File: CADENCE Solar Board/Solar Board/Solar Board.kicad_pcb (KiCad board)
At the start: 2 copper layers, 36 parts, among them J1 Conn_01x08, U1 INA230AIRGTT, U2 AD7414ARTZ-1REEL7, U3 OPT3001IDNPRQ1

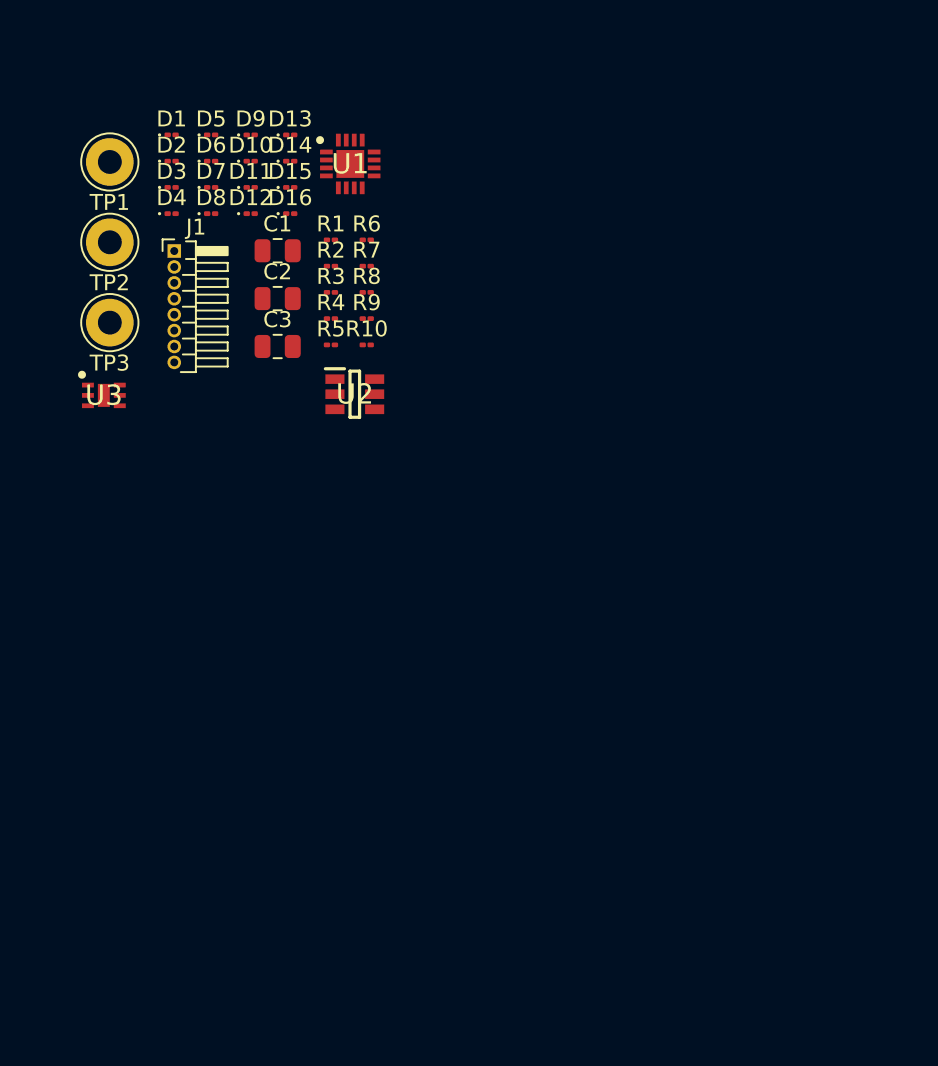
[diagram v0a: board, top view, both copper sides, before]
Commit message: fixed diodes
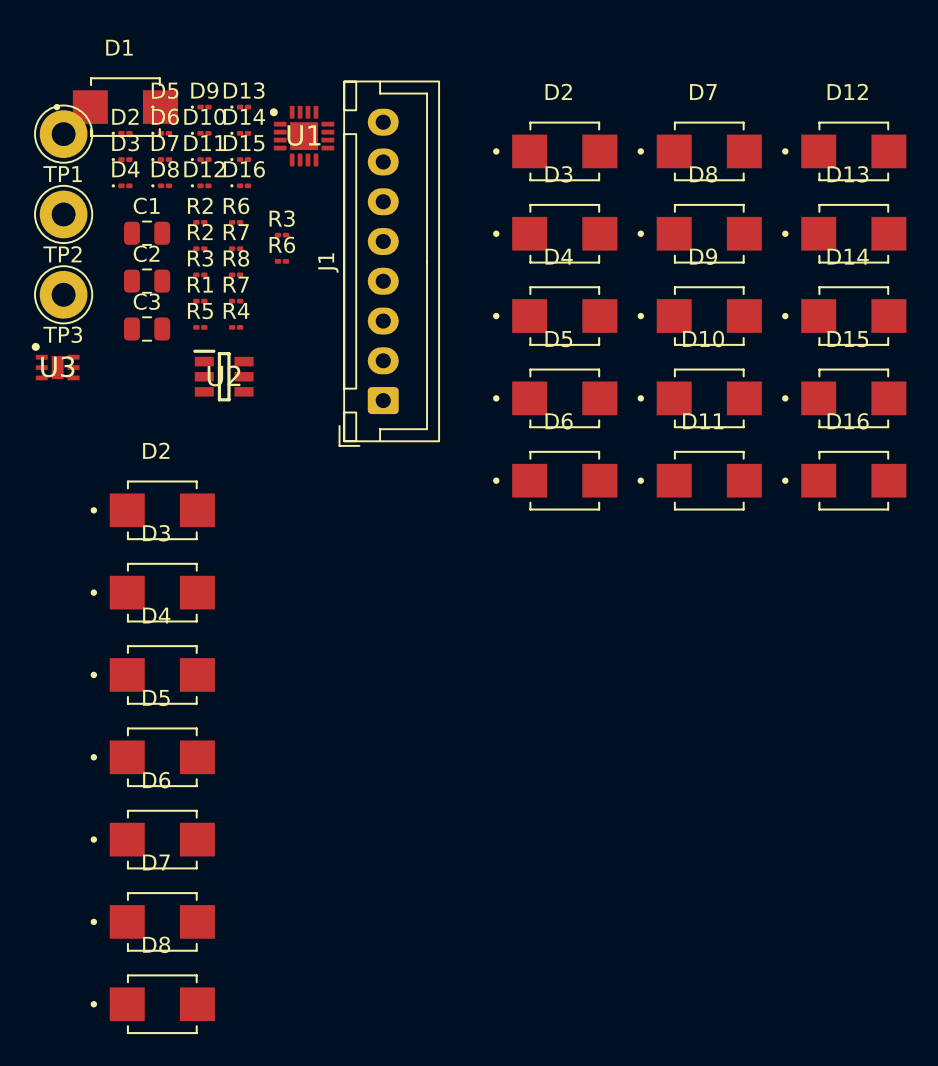
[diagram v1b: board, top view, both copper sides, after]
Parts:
- added D10: D, SK44BL-TP:DIOM4336X265N, F.Cu at (55.6, 31.6)
- added D11: D, SK44BL-TP:DIOM4336X265N, F.Cu at (55.6, 36.8)
- added D12: D, SK44BL-TP:DIOM4336X265N, F.Cu at (64.7, 16.1)
- added D13: D, SK44BL-TP:DIOM4336X265N, F.Cu at (64.7, 21.3)
- added D14: D, SK44BL-TP:DIOM4336X265N, F.Cu at (64.7, 26.4)
- added D15: D, SK44BL-TP:DIOM4336X265N, F.Cu at (64.7, 31.6)
- added D16: D, SK44BL-TP:DIOM4336X265N, F.Cu at (64.7, 36.8)
- added D2: D, SK44BL-TP:DIOM4336X265N, F.Cu at (46.5, 16.1)
- added D2: D, SK44BL-TP:DIOM4336X265N, F.Cu at (21.2, 38.6)
- added D3: D, SK44BL-TP:DIOM4336X265N, F.Cu at (21.2, 43.8)
- added D3: D, SK44BL-TP:DIOM4336X265N, F.Cu at (46.5, 21.3)
- added D4: D, SK44BL-TP:DIOM4336X265N, F.Cu at (46.5, 26.4)
- added D4: D, SK44BL-TP:DIOM4336X265N, F.Cu at (21.2, 49.0)
- added D5: D, SK44BL-TP:DIOM4336X265N, F.Cu at (21.2, 54.2)
- added D5: D, SK44BL-TP:DIOM4336X265N, F.Cu at (46.5, 31.6)
- added D6: D, SK44BL-TP:DIOM4336X265N, F.Cu at (46.5, 36.8)
- added D6: D, SK44BL-TP:DIOM4336X265N, F.Cu at (21.2, 59.4)
- added D7: D, SK44BL-TP:DIOM4336X265N, F.Cu at (55.6, 16.1)
- added D7: D, SK44BL-TP:DIOM4336X265N, F.Cu at (21.2, 64.5)
- added D8: D, SK44BL-TP:DIOM4336X265N, F.Cu at (55.6, 21.3)
- added D8: D, SK44BL-TP:DIOM4336X265N, F.Cu at (21.2, 69.7)
- added D9: D, SK44BL-TP:DIOM4336X265N, F.Cu at (55.6, 26.4)
- added R3: 500, Resistor_SMD:R_01005_0402Metric, F.Cu at (28.7, 21.4)
- added R6: 500, Resistor_SMD:R_01005_0402Metric, F.Cu at (28.7, 23.0)
- D1: footprint Diode_SMD:D_01005_0402Metric -> SK44BL-TP:DIOM4336X265N
- J1: footprint Connector_PinHeader_1.00mm:PinHeader_1x08_P1.00mm_Horizontal -> Connector_JST:JST_XH_B8B-XH-A_1x08_P2.50mm_Vertical
- moved J1 16.2 mm to (35.1, 31.8), turned to 90 degrees
- moved R1 8.28 mm to (23.6, 25.5)
- moved R2 8.28 mm to (23.6, 20.6)
- moved R2 8.28 mm to (23.6, 22.2)
- moved R3 8.28 mm to (23.6, 23.9)
- moved R4 8.28 mm to (25.8, 27.1)
- moved R5 8.28 mm to (23.6, 27.1)
- moved R6 8.28 mm to (25.8, 20.6)
- moved R7 8.28 mm to (25.8, 22.2)
- moved R7 8.28 mm to (25.8, 25.5)
- moved R8 8.28 mm to (25.8, 23.9)
- moved U2 8.28 mm to (25.1, 30.2)
- moved C1 8.28 mm to (20.2, 21.2)
- moved C2 8.28 mm to (20.2, 24.2)
- moved C3 8.28 mm to (20.2, 27.2)
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- renumbered R4 to R1, R1 to R2, R10 to R4, R9 to R7
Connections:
- C2 pad 1: Net-(U2-ALERT) -> +3.3V
- C3 pad 1: Net-(U2-ALERT) -> +3.3V
- R1 pad 2: Net-(U1-IN+) -> Solar1+
- R7 pad 2: Net-(U2-ALERT) -> +3.3V
- U1 pad 13: Net-(U1-IN+) -> Solar1+
- U1 pad 4: Net-(U1-SDA) -> HS_I2C1_LDA
- U1 pad 5: Net-(U1-SCL) -> HS_I2C1_LCL
- U2 pad 4: Net-(U2-SCL) -> HS_I2C1_LCL
- U2 pad 6: Net-(U2-SDA) -> HS_I2C1_LDA

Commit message: minor pcb and schematic updates
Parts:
- removed D10, D11, D12, D13, D14, D15, D16, D3, D4, D5, D6, D7, D8, D9: D, Diode_SMD:D_01005_0402Metric
- removed D10, D11, D12, D13, D14, D15, D16, D3 (x2), D4 (x2), D5 (x2), D6 (x2), D7 (x2), D8 (x2), D9: D, SK44BL-TP:DIOM4336X265N
- removed the D2 at (46.5, 16.1)
- removed the D2 at (18.9, 14.9)
- removed the D2 at (21.2, 38.6)
- removed the R2 at (23.6, 20.6)
- removed the R2 at (23.6, 22.2)
- removed the R3 at (23.6, 23.9)
- removed the R3 at (28.7, 21.4)
- removed the R6 at (28.7, 23.0)
- removed the R6 at (25.8, 20.6)
- removed the R7 at (25.8, 22.2)
- removed the R7 at (25.8, 25.5)
- added D2: LED, LED_SMD:LED_RGB_Lumex_SML-LXT0805SIUGUBW, F.Cu at (36.3, 33.4)
- added R2: 10k, Resistor_SMD:R_0805_2012Metric, F.Cu at (25.8, 55.0)
- added R3: 500, Resistor_SMD:R_0805_2012Metric, F.Cu at (21.2, 55.0)
- added R6: 500, Resistor_SMD:R_0805_2012Metric, F.Cu at (26.0, 33.0)
- added R7: 1k, Resistor_SMD:R_0805_2012Metric, F.Cu at (26.5, 39.0)
- D1: value D -> LED; footprint SK44BL-TP:DIOM4336X265N -> LED_SMD:LED_RGB_Lumex_SML-LXT0805SIUGUBW
- R1, R4, R5, R8: footprint Resistor_SMD:R_01005_0402Metric -> Resistor_SMD:R_0805_2012Metric
- moved TP1 45.1 mm to (25.0, 59.0)
- moved D1 41.8 mm to (16.2, 55.0)
- moved U1 40.4 mm to (31.2, 55.5)
- moved U3 37.9 mm to (52.5, 30.5)
- moved R4 31.8 mm to (36.8, 57.0)
- moved R1 30.1 mm to (35.8, 53.0)
- moved C1 29.8 mm to (50.0, 20.6)
- moved R5 26.3 mm to (48.0, 37.0)
- moved R8 21.7 mm to (46.7, 29.8)
- moved J1 21.3 mm to (19.0, 17.9), turned to 0 degrees
- moved U2 16.8 mm to (41.2, 35.0)
- moved C2 13.9 mm to (31.8, 31.9)
- moved C3 13.9 mm to (31.8, 35.0)
- moved TP2 10.3 mm to (18.0, 29.9)
- moved TP3 10.3 mm to (18.0, 34.9)
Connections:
- D1 pad 1: Net-(D1-K) -> GND
- R5 pad 1: HS_I2C1_LCL -> +3.3V
- R5 pad 2: Net-(U2-SCL) -> Net-(U2-ALERT)

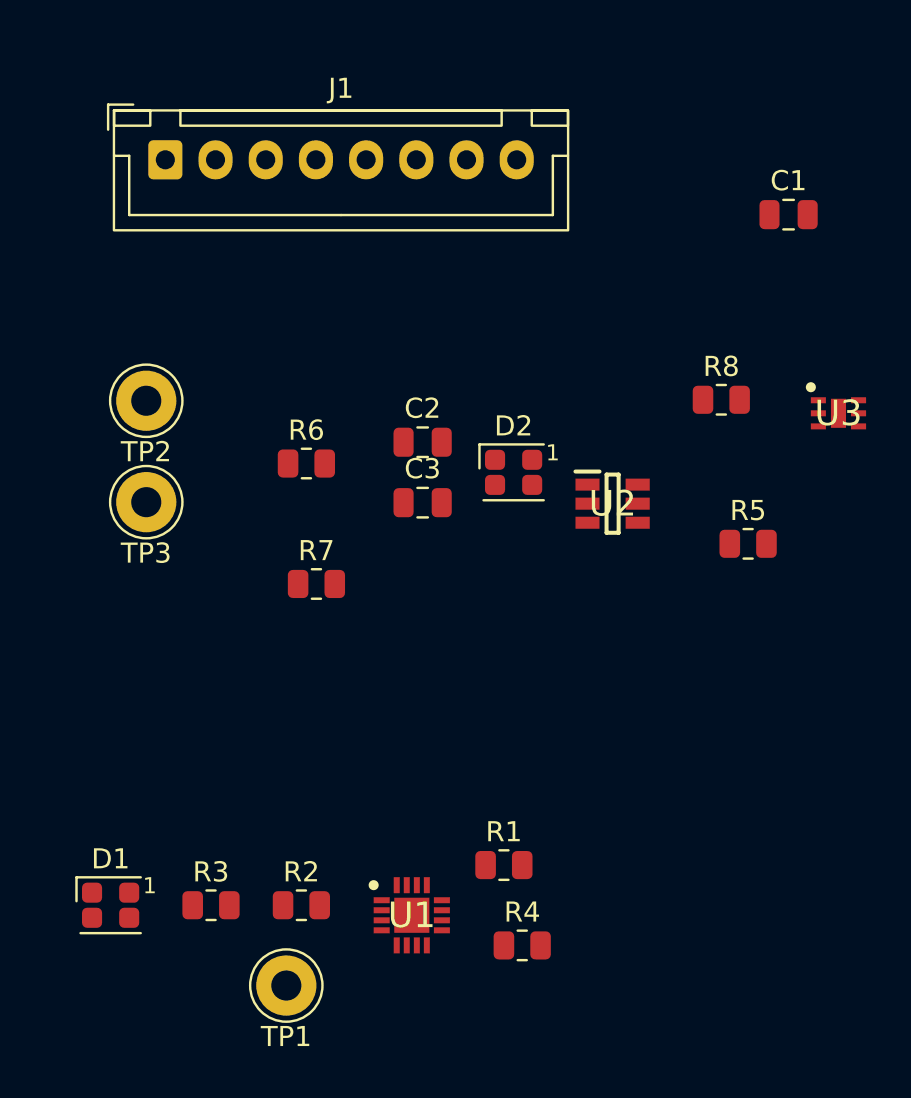
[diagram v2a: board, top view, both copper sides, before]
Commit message: PCB Optimized (made smaller)
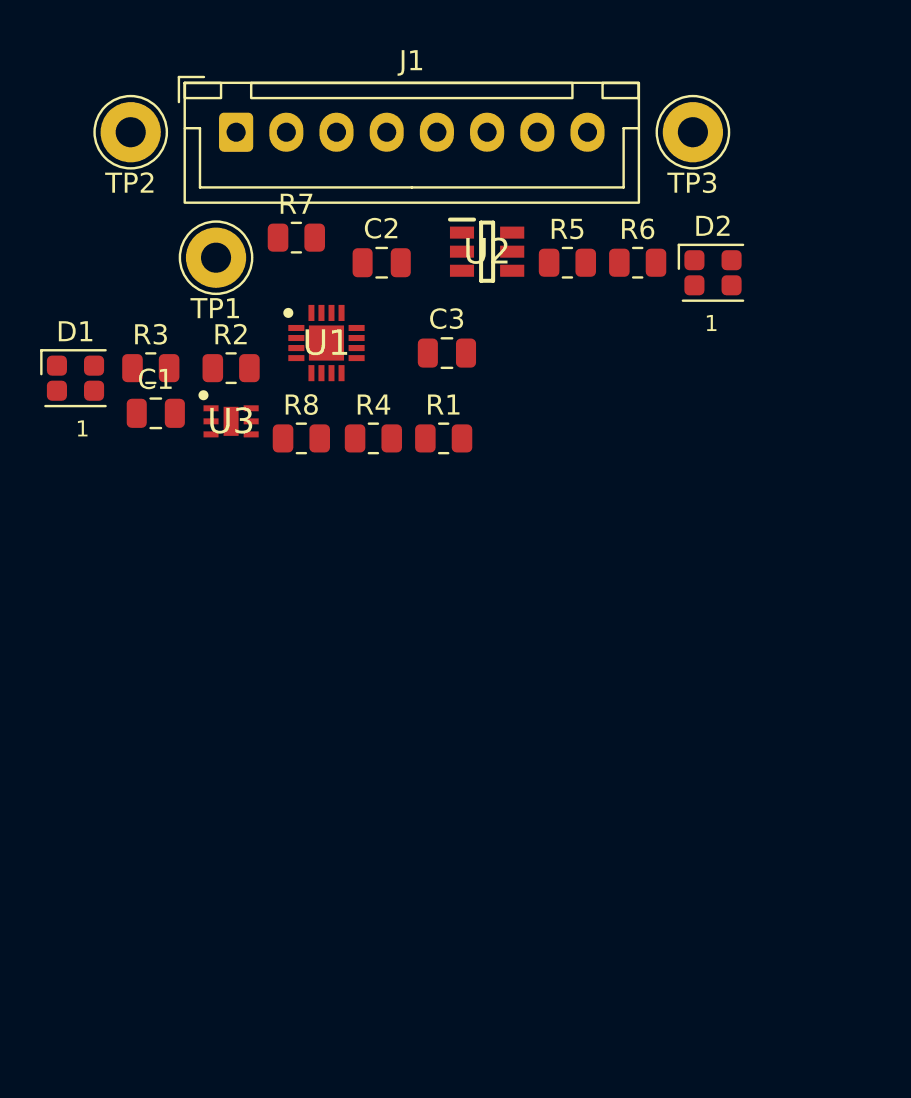
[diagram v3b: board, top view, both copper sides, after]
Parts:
- moved TP1 36.4 mm to (21.5, 22.8)
- moved C1 33.0 mm to (18.5, 30.5)
- moved TP3 32.9 mm to (45.2, 16.5)
- moved U3 30.3 mm to (22.2, 30.9)
- moved U1 28.8 mm to (27.0, 27.0)
- moved R2 27.0 mm to (22.2, 28.2)
- moved R3 26.9 mm to (18.2, 28.2)
- moved R4 26.3 mm to (29.3, 31.8)
- moved D1 26.3 mm to (14.5, 28.8)
- moved R1 21.5 mm to (32.8, 31.8)
- moved R8 21.0 mm to (25.8, 31.8)
- moved R6 19.3 mm to (42.5, 23.0)
- moved R7 17.3 mm to (25.5, 21.8)
- moved R5 16.6 mm to (39.0, 23.0)
- moved D2 14.1 mm to (46.2, 23.5)
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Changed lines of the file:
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@@
 	(footprint "Resistor_SMD:R_0805_2012Metric"
 		(layer "F.Cu")
-		(at 25.75 55)
+		(at 22.25 28.25)
 		(descr "Resistor SMD 0805 (2012 Metric), square (rectangular) end terminal, IPC-7351 nominal, (Body size source: IPC-SM-782 page 72, https://www.pcb-3d.com/wordpress/wp-content/uploads/ipc-sm-782a_amendment_1_and_2.pdf)")
 		(tags "resistor")
@@
 	(footprint "Connector_Pin:Pin_D1.3mm_L11.0mm_LooseFit"
 		(layer "F.Cu")
-		(at 18.025 34.925)
+		(at 45.25 16.5)
 		(descr "solder Pin_ diameter 1.3mm, hole diameter 1.5mm (loose fit), length 11.0mm")
 		(tags "solder Pin_ loose fit")
@@
 	(footprint "INA230AIRGTT:QFN50P300X300X100-17N-D"
 		(layer "F.Cu")
-		(at 31.25 55.5)
+		(at 27 27)
 		(descr "RGT0016C height=1")
 		(tags "Integrated Circuit")
@@
 	(footprint "AD7414ARTZ-1REEL7:SOT95P280X145-6N"
 		(layer "F.Cu")
-		(at 41.25 35)
+		(at 35 22.45)
 		(descr "(RJ-6)")
 		(tags "Integrated Circuit")
@@
 	(footprint "Connector_JST:JST_XH_B8B-XH-A_1x08_P2.50mm_Vertical"
 		(layer "F.Cu")
-		(at 18.975 17.875)
+		(at 22.5 16.5)
 		(descr "JST XH series connector, B8B-XH-A (http://www.jst-mfg.com/product/pdf/eng/eXH.pdf)")
 		(tags "connector JST XH vertical")
@@
 	(footprint "LED_SMD:LED_RGB_Lumex_SML-LXT0805SIUGUBW"
 		(layer "F.Cu")
-		(at 36.32 33.44)
+		(at 46.25 23.5)
 		(descr "RGB LED 0805 2.0mm x 1.3mm, orientation marker at common anode https://www.mouser.de/datasheet/2/244/SML-LXT0805SIUGUBW-1776540.pdf")
 		(tags "RGB LED 0805")
@@
 		)
 		(fp_text user "1"
-			(at 1.6 -0.5 0)
+			(at -0.425 3 0)
 			(unlocked yes)
 			(layer "F.SilkS")
@@
 	(footprint "Capacitor_SMD:C_0805_2012Metric"
 		(layer "F.Cu")
-		(at 31.79 31.94)
+		(at 29.75 23)
 		(descr "Capacitor SMD 0805 (2012 Metric), square (rectangular) end terminal, IPC-7351 nominal, (Body size source: IPC-SM-782 page 76, https://www.pcb-3d.com/wordpress/wp-content/uploads/ipc-sm-782a_amendment_1_and_2.pdf, https://docs.google.com/spreadsheets/d/1BsfQQcO9C6DZCsRaXUlFlo91Tg2WpOkGARC1WS5S8t0/edit?usp=sharing)")
 		(tags "capacitor")
@@
 	(footprint "Capacitor_SMD:C_0805_2012Metric"
 		(layer "F.Cu")
-		(at 31.79 34.95)
+		(at 33 27.5)
 		(descr "Capacitor SMD 0805 (2012 Metric), square (rectangular) end terminal, IPC-7351 nominal, (Body size source: IPC-SM-782 page 76, https://www.pcb-3d.com/wordpress/wp-content/uploads/ipc-sm-782a_amendment_1_and_2.pdf, https://docs.google.com/spreadsheets/d/1BsfQQcO9C6DZCsRaXUlFlo91Tg2WpOkGARC1WS5S8t0/edit?usp=sharing)")
 		(tags "capacitor")
@@
 	(footprint "Resistor_SMD:R_0805_2012Metric"
 		(layer "F.Cu")
-		(at 35.8375 53)
+		(at 32.8375 31.75)
 		(descr "Resistor SMD 0805 (2012 Metric), square (rectangular) end terminal, IPC-7351 nominal, (Body size source: IPC-SM-782 page 72, https://www.pcb-3d.com/wordpress/wp-content/uploads/ipc-sm-782a_amendment_1_and_2.pdf)")
 		(tags "resistor")
@@
 	(footprint "Capacitor_SMD:C_0805_2012Metric"
 		(layer "F.Cu")
-		(at 50.015 20.605)
+		(at 18.5 30.5)
 		(descr "Capacitor SMD 0805 (2012 Metric), square (rectangular) end terminal, IPC-7351 nominal, (Body size source: IPC-SM-782 page 76, https://www.pcb-3d.com/wordpress/wp-content/uploads/ipc-sm-782a_amendment_1_and_2.pdf, https://docs.google.com/spreadsheets/d/1BsfQQcO9C6DZCsRaXUlFlo91Tg2WpOkGARC1WS5S8t0/edit?usp=sharing)")
 		(tags "capacitor")
@@
 	(footprint "Resistor_SMD:R_0805_2012Metric"
 		(layer "F.Cu")
-		(at 36.75 57)
+		(at 29.3375 31.75)
 		(descr "Resistor SMD 0805 (2012 Metric), square (rectangular) end terminal, IPC-7351 nominal, (Body size source: IPC-SM-782 page 72, https://www.pcb-3d.com/wordpress/wp-content/uploads/ipc-sm-782a_amendment_1_and_2.pdf)")
 		(tags "resistor")
@@
 	(footprint "OPT3001IDNPRQ1:SON65P200X200X65-7N-D"
 		(layer "F.Cu")
-		(at 52.5 30.5)
+		(at 22.25 30.9)
 		(descr "OPT3001IDNPRQ1-1")
 		(tags "Integrated Circuit")
@@
 	(footprint "Resistor_SMD:R_0805_2012Metric"
 		(layer "F.Cu")
-		(at 46.665 29.825)
+		(at 25.75 31.75)
 		(descr "Resistor SMD 0805 (2012 Metric), square (rectangular) end terminal, IPC-7351 nominal, (Body size source: IPC-SM-782 page 72, https://www.pcb-3d.com/wordpress/wp-content/uploads/ipc-sm-782a_amendment_1_and_2.pdf)")
 		(tags "resistor")
@@
 	(footprint "LED_SMD:LED_RGB_Lumex_SML-LXT0805SIUGUBW"
 		(layer "F.Cu")
-		(at 16.25 55)
+		(at 14.5 28.75)
 		(descr "RGB LED 0805 2.0mm x 1.3mm, orientation marker at common anode https://www.mouser.de/datasheet/2/244/SML-LXT0805SIUGUBW-1776540.pdf")
 		(tags "RGB LED 0805")
@@
 		)
 		(fp_text user "1"
-			(at 1.6 -0.5 0)
+			(at 0 3 0)
 			(unlocked yes)
 			(layer "F.SilkS")
@@
 	(footprint "Connector_Pin:Pin_D1.3mm_L11.0mm_LooseFit"
 		(layer "F.Cu")
-		(at 25 59)
+		(at 21.5 22.75)
 		(descr "solder Pin_ diameter 1.3mm, hole diameter 1.5mm (loose fit), length 11.0mm")
 		(tags "solder Pin_ loose fit")
@@
 	(footprint "Resistor_SMD:R_0805_2012Metric"
 		(layer "F.Cu")
-		(at 26.5 39)
+		(at 25.5 21.75)
 		(descr "Resistor SMD 0805 (2012 Metric), square (rectangular) end terminal, IPC-7351 nominal, (Body size source: IPC-SM-782 page 72, https://www.pcb-3d.com/wordpress/wp-content/uploads/ipc-sm-782a_amendment_1_and_2.pdf)")
 		(tags "resistor")
@@
 	(footprint "Resistor_SMD:R_0805_2012Metric"
 		(layer "F.Cu")
-		(at 26 33)
+		(at 42.5 23)
 		(descr "Resistor SMD 0805 (2012 Metric), square (rectangular) end terminal, IPC-7351 nominal, (Body size source: IPC-SM-782 page 72, https://www.pcb-3d.com/wordpress/wp-content/uploads/ipc-sm-782a_amendment_1_and_2.pdf)")
 		(tags "resistor")
@@
 	(footprint "Resistor_SMD:R_0805_2012Metric"
 		(layer "F.Cu")
-		(at 21.25 55)
+		(at 18.25 28.25)
 		(descr "Resistor SMD 0805 (2012 Metric), square (rectangular) end terminal, IPC-7351 nominal, (Body size source: IPC-SM-782 page 72, https://www.pcb-3d.com/wordpress/wp-content/uploads/ipc-sm-782a_amendment_1_and_2.pdf)")
 		(tags "resistor")
@@
 	(footprint "Resistor_SMD:R_0805_2012Metric"
 		(layer "F.Cu")
-		(at 48 37)
+		(at 39 23)
 		(descr "Resistor SMD 0805 (2012 Metric), square (rectangular) end terminal, IPC-7351 nominal, (Body size source: IPC-SM-782 page 72, https://www.pcb-3d.com/wordpress/wp-content/uploads/ipc-sm-782a_amendment_1_and_2.pdf)")
 		(tags "resistor")
@@
 	(footprint "Connector_Pin:Pin_D1.3mm_L11.0mm_LooseFit"
 		(layer "F.Cu")
-		(at 18.025 29.875)
+		(at 17.25 16.5)
 		(descr "solder Pin_ diameter 1.3mm, hole diameter 1.5mm (loose fit), length 11.0mm")
 		(tags "solder Pin_ loose fit")

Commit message: PCB updates
added custom solar cell footprints and created base layer for the thin PCB board
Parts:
- added SC: CAVU Solar Cell, Solar Cell Library:CAVU Solar Cell, F.Cu at (110.5, 320.0)
- added SC: CAVU Solar Cell, Solar Cell Library:CAVU Solar Cell, F.Cu at (110.5, 80.0)
- added SC: CAVU Solar Cell, Solar Cell Library:CAVU Solar Cell, F.Cu at (110.5, 160.0)
- added SC: CAVU Solar Cell, Solar Cell Library:CAVU Solar Cell, F.Cu at (24.3, 150.0)
- added SC: CAVU Solar Cell, Solar Cell Library:CAVU Solar Cell, F.Cu at (24.3, 230.0)
- added SC: CAVU Solar Cell, Solar Cell Library:CAVU Solar Cell, F.Cu at (24.3, 310.0)
- added SC: CAVU Solar Cell, Solar Cell Library:CAVU Solar Cell, F.Cu at (110.5, 240.0)
- added SC: CAVU Solar Cell, Solar Cell Library:CAVU Solar Cell, F.Cu at (24.2, 69.8)
- moved U2 171.8 mm to (71.1, 190.4)
- moved C1 171.8 mm to (54.6, 198.5)
- moved C2 171.8 mm to (65.8, 191.0)
- moved C3 171.8 mm to (69.1, 195.5)
- moved D1 171.8 mm to (50.6, 196.7)
- moved D2 171.8 mm to (82.3, 191.5)
- moved J1 171.8 mm to (58.6, 184.5)
- moved R1 171.8 mm to (68.9, 199.7)
- moved R2 171.8 mm to (58.4, 196.2)
- moved R3 171.8 mm to (54.4, 196.2)
- moved R4 171.8 mm to (65.4, 199.7)
- moved R5 171.8 mm to (75.1, 191.0)
- moved R6 171.8 mm to (78.6, 191.0)
- moved R7 171.8 mm to (61.6, 189.7)
- moved R8 171.8 mm to (61.9, 199.7)
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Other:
- board outline added: 100 x 351 mm

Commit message: PCB updates
added traces, moved location
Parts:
- C1, C2, C3, D1, D2, J1, R1, R2, R3, R4, R5, R6, R7, R8, TP1, TP2, TP3, U1, U2, U3: moved to B.Cu
- moved C1 177.0 mm to (81.8, 23.6), turned to 180 degrees
- moved R8 176.4 mm to (77.0, 24.0)
- moved U3 175.5 mm to (73.5, 24.0)
- moved D2 172.3 mm to (52.0, 21.9), turned to 180 degrees
- moved C3 172.1 mm to (68.3, 23.4), turned to 180 degrees
- moved R1 171.5 mm to (78.5, 28.5), turned to 180 degrees
- moved R4 171.5 mm to (75.0, 28.5)
- moved R6 171.1 mm to (55.7, 21.4)
- moved C2 171.1 mm to (72.5, 20.0), turned to 180 degrees
- moved R7 170.4 mm to (68.5, 19.5)
- moved R5 170.3 mm to (59.2, 21.4)
- moved U2 169.8 mm to (63.2, 20.8), turned to 180 degrees
- moved D1 168.3 mm to (58.6, 28.6), turned to 180 degrees
- moved R3 167.9 mm to (62.5, 28.5)
- moved R2 167.9 mm to (66.0, 28.5), turned to 180 degrees
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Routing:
- net HS_I2C1_LDA: track 0.00 -> 37.9 mm, vias 0 -> 5
- net HS_I2C1_LCL: track 0.00 -> 27.9 mm, vias 0 -> 2
- net Solar1+: track 0.00 -> 18.0 mm
- net Net-(U2-ALERT): track 0.00 -> 7.62 mm
- net Net-(U1-ALERT): track 0.00 -> 7.58 mm
- net Solar1-: track 0.00 -> 4.98 mm
- net Net-(U2-AS): track 0.00 -> 3.67 mm
- net Net-(D1-A): track 0.00 -> 2.71 mm
- net Net-(U1-V_S+): track 0.00 -> 2.37 mm
- net Net-(D2-A): track 0.00 -> 1.96 mm
- net Net-(U3-INT): track 0.00 -> 1.59 mm
- net GND: track 0.00 -> 1.44 mm
- added copper zone on B.Cu, net +3.3V
- added copper zone on F.Cu, net GND
